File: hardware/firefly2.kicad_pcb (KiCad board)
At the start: 2 copper layers, 41.4 x 41.3 mm, 19 parts, among them J1 Conn_01x01, J2 614105150721, J3 CONN_01X01, P2 CONN_01X03, P3 CONN_01X04, P4 CONN_01X05, P5 CONN_01X01, U1 SAMD21E18, U2 RFM69CW, U3 MIC5504

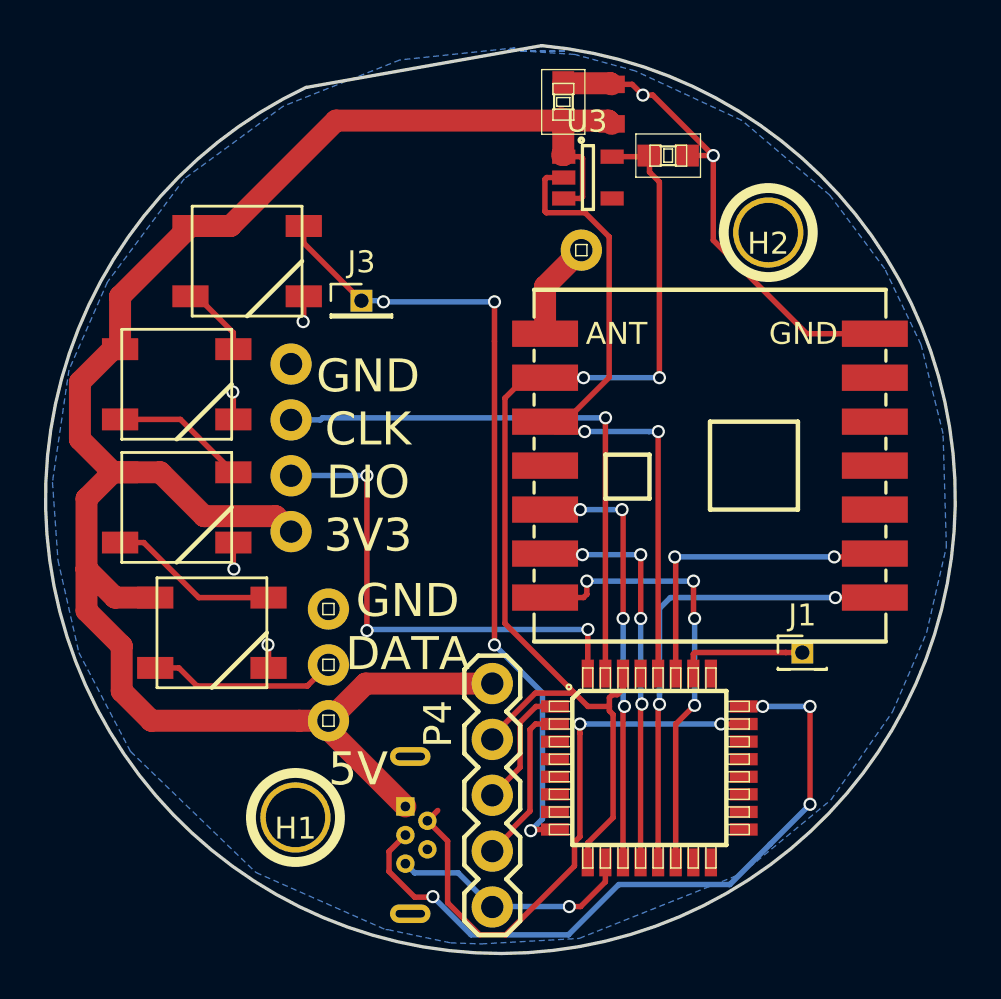
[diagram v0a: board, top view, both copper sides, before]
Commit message: Hardware revision 2.4:
- Add buffer to bump LED signal to input voltage
- Add pads between reset and ground, to facilitate testing

Change-Id: If3ba1aed20585e03bd6f188c24cdaebd21a51b41
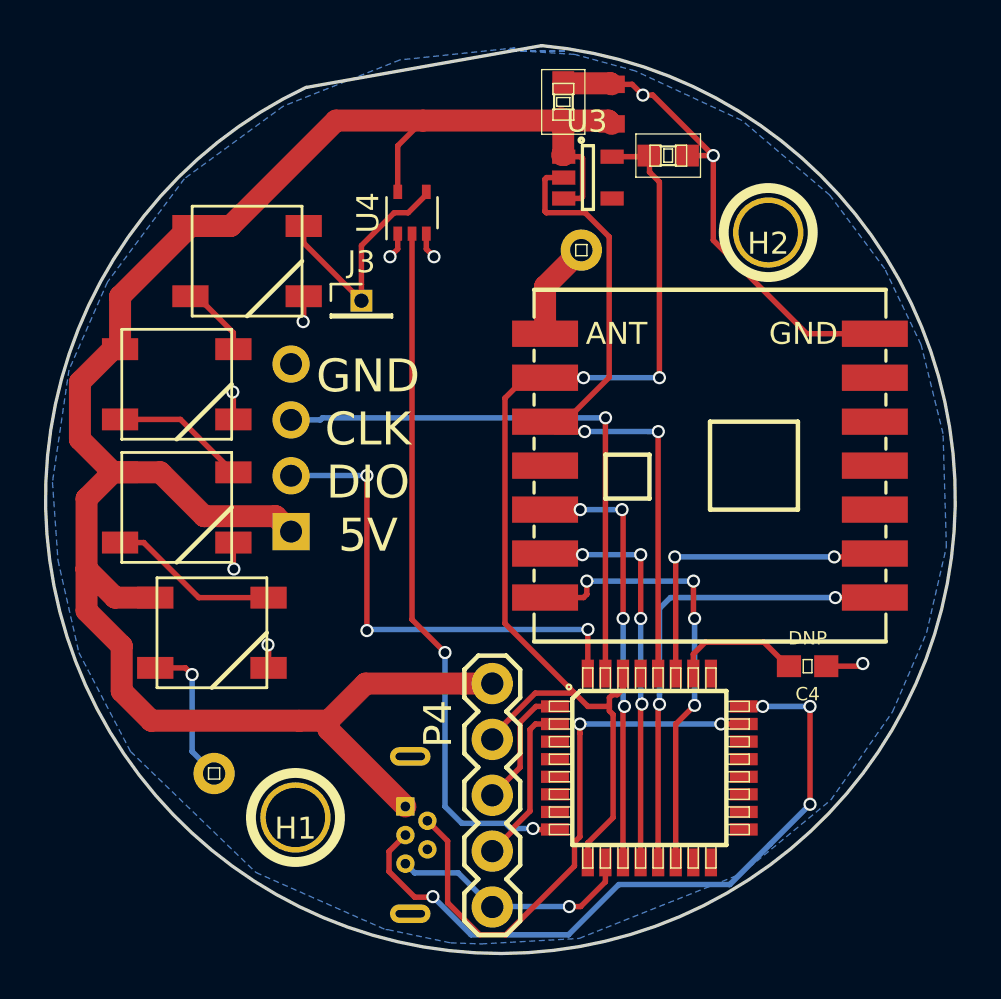
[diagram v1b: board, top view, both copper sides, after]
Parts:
- removed J1: Conn_01x01, Pin_Headers:Pin_Header_Straight_1x01_Pitch1.27mm
- removed P2: CONN_01X03, SparkFun-Connectors:1X03
- added C4: DNP, SparkFun-Capacitors:0603, F.Cu at (174.0, 71.1)
- added P5: CONN_01X01, SparkFun-Connectors:1X01, F.Cu at (147.0, 76.0)
- added U4: 74LVC1G125, TO_SOT_Packages_SMD:SOT-353_SC-70-5, F.Cu at (156.0, 50.5)
- P3: footprint Sparkfun-Connectors:1X04 -> Pin_Headers:Pin_Header_Straight_1x04_Pitch2.54mm
- turned P3 to 0 degrees
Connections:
- D1 pad 4: LED_INTERNAL -> Net-(D1-Pad4)
- J3 pad 1: LED_INTERNAL -> Net-(D1-Pad4)
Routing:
- net Net-(D1-Pad4): track 0.00 -> 11.0 mm
- net LED_INTERNAL: track 36.9 -> 32.1 mm, vias 4 -> 2
- net GND: track 73.5 -> 77.3 mm, vias 9 -> 12
- net +5V: track 88.7 -> 92.4 mm
- net LED_EXTERNAL: track 8.62 -> 6.72 mm, vias 0 -> 1
- net USB_D-: track 26.4 -> 25.8 mm
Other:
- board text added: "GND CLK DIO 5V"
- board text removed: "5V"
- board text removed: "GND CLK DIO 3V3"
- board text removed: "GND DATA"

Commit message: Fix version number to 2.4 on silk
Change-Id: I5ba1420b467663fdf9ea06c879421b5f0d6014bd
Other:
- board text added: "Firefly V2.4"
- board text removed: "Firefly V2.1"
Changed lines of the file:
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@@
     (links 53)
     (no_connects 0)
-    (area 139.25939 42.824999 180.78061 84.26061)
+    (area 139.25939 42.824999 187.034459 84.714286)
     (thickness 1.6)
     (drawings 139)
@@
     (34 B.Paste user hide)
     (35 F.Paste user hide)
-    (36 B.SilkS user hide)
+    (36 B.SilkS user)
     (37 F.SilkS user)
     (38 B.Mask user hide)
@@
     (effects (font (size 1.5 1.5) (thickness 0.3)) (justify left mirror))
   )
-  (gr_text "Firefly V2.1" (at 155.5 52.45) (layer B.SilkS)
+  (gr_text "Firefly V2.4" (at 155.5 52.45) (layer B.SilkS)
     (effects (font (size 1.5 1.5) (thickness 0.3)) (justify mirror))
   )

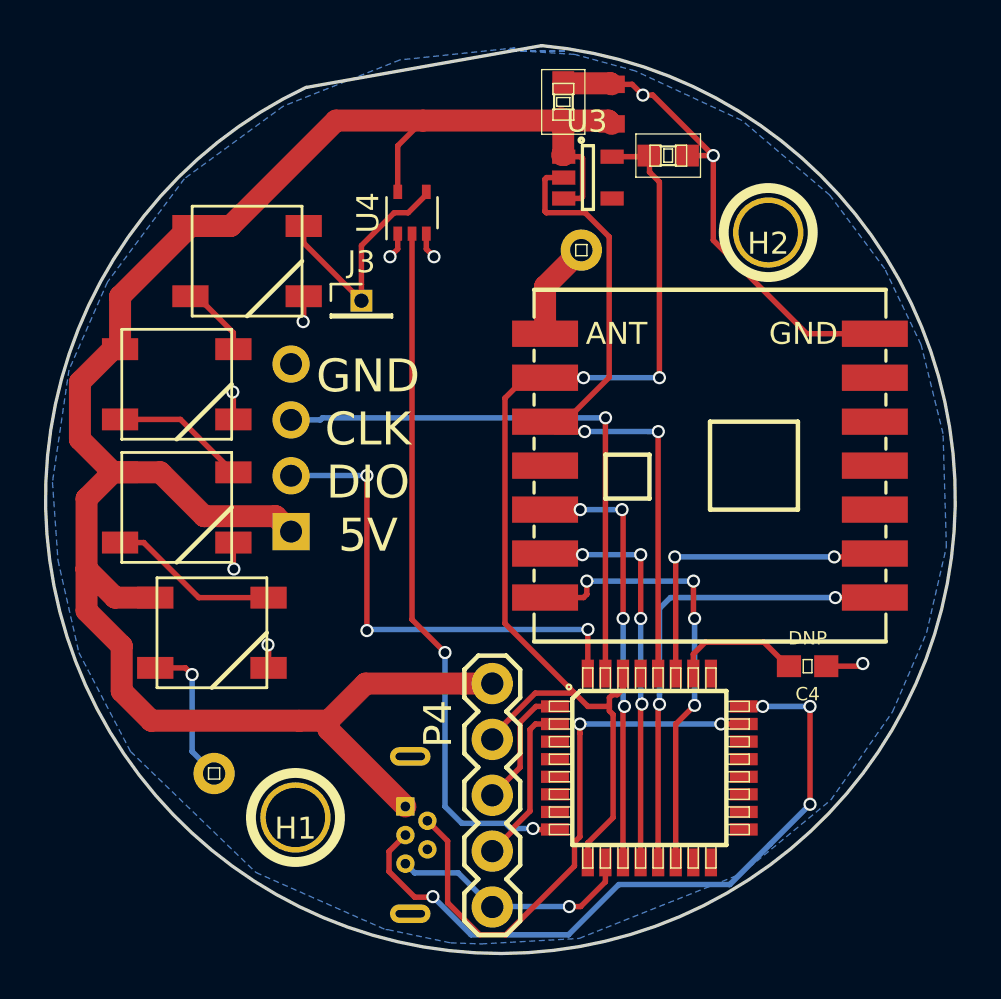
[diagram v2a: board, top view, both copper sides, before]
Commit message: Hard v2.5:
- Add a power eater circuit to keep USB batteries on

Change-Id: I22aef8479abf481f47f24733b5794af7d33fd833
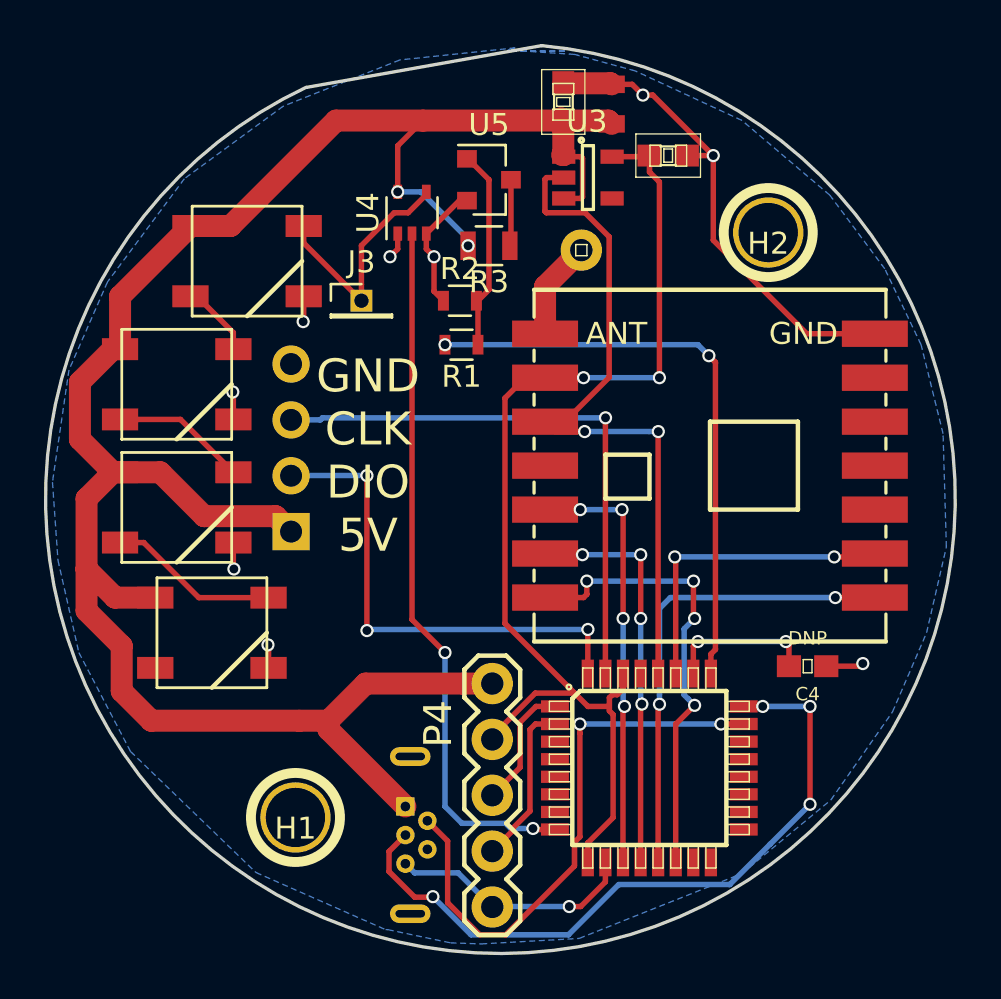
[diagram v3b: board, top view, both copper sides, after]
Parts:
- removed the P5 at (147.0, 76.0)
- added R1: 470, Resistors_SMD:R_0603, F.Cu at (158.2, 56.5)
- added R2: 10k, Resistors_SMD:R_0603, F.Cu at (158.2, 54.5)
- added R3: 20, Resistors_SMD:R_0805, F.Cu at (159.5, 52.0)
- added U5: MOSFET, TO_SOT_Packages_SMD:SOT-23, F.Cu at (159.5, 49.0)
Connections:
- D4 pad 2: LED_EXTERNAL -> Net-(D4-Pad2)
- U1 pad 25: Net-(U1-Pad25) -> POWER_EATER
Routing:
- net POWER_EATER: track 0.00 -> 26.9 mm, vias 0 -> 2
- net Net-(R1-Pad1): track 0.00 -> 9.10 mm
- net LED_EXTERNAL: track 6.72 -> 0.00 mm, vias 1 -> 0
- net GND: track 77.3 -> 82.0 mm
- net +5V: track 92.4 -> 96.8 mm, vias 0 -> 2
- net Net-(R3-Pad1): track 0.00 -> 3.02 mm
- net Net-(C4-Pad2): track 5.91 -> 6.77 mm, vias 0 -> 2
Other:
- board text added: "10uF"
- board text added: "1uF"
- board text added: "DNP"
- board text added: "Firefly V2.5"
- board text removed: "Firefly V2.4"
